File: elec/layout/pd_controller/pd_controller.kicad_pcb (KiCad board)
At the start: 2 copper layers, 26.4 x 17.6 mm, 17 parts, among them Q1 MOSFET, U1 STUSB4500QTR

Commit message: layout 95%
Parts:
- moved Q1 47.5 mm to (168.4, 57.5)
- moved R2 47.5 mm to (169.1, 66.6)
- moved R7 47.5 mm to (174.1, 61.5)
- moved U1 47.5 mm to (171.0, 63.2)
- moved C1 47.5 mm to (164.7, 54.3)
- moved C2 47.5 mm to (174.1, 60.3)
- moved D1 47.5 mm to (167.9, 60.4)
- moved R6 47.5 mm to (174.1, 62.6)
- moved USB1 47.5 mm to (163.0, 60.2)
- moved R1 47.5 mm to (171.2, 66.6)
- moved C3 47.5 mm to (171.4, 60.0)
- moved C4 47.5 mm to (170.4, 60.0)
- moved D2 47.5 mm to (167.5, 55.0)
- moved D3 47.5 mm to (170.5, 55.0)
- moved R4 47.5 mm to (172.9, 60.3)
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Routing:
- net VBUS: track 22.2 -> 0.00 mm, vias 11 -> 0
- net (no net): track 22.2 -> 0.00 mm, vias 2 -> 0
- net I2C_SCL: track 15.2 -> 0.00 mm, vias 2 -> 0
- net lv: track 12.7 -> 0.00 mm, vias 30 -> 0
- net I2C_SDA: track 11.6 -> 0.00 mm, vias 2 -> 0
- net 32: track 0.00 -> 9.23 mm
- net VSINK_VCC: track 7.14 -> 0.00 mm
- net CC2: track 5.99 -> 0.00 mm
- net CC1: track 5.72 -> 0.00 mm
- net 36: track 0.00 -> 4.51 mm
- net 31: track 0.00 -> 3.80 mm
- net 27: track 0.00 -> 2.86 mm
- net 28: track 0.00 -> 2.83 mm
- net USB_CONNECTOR-net-1: track 2.72 -> 0.00 mm
- net USB_CONNECTOR-net: track 2.72 -> 0.00 mm
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
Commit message: Build full
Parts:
- removed USB1: TYPE_C_16PIN_2MD073, lcsc:USB-C-SMD_TYPE-C-6PIN-2MD-073
- C2: value 100nF ±10% 10V X5R -> 1µF ±10% 10V X5R; footprint lcsc:C0201 -> lcsc:C0402
- C3: value 1µF ±20% 6.3V X5R -> 1µF ±10% 10V X5R; footprint lcsc:C0201 -> lcsc:C0402
- C4: value (none) -> 100nF ±10% 16V X7R; footprint lcsc:C0201 -> lcsc:C0402
- D2, D3: value (none) -> infV
- Q1: footprint lcsc:SOT-23-3_L2.9-W1.3-P1.90-LS2.4-BR -> lcsc:PDFN3333-8_L3.1-W3.2-P0.65-LS3.4-BL
- R1: value 1kΩ ±1% 50mW -> 1kΩ ±1% 62.5mW; footprint lcsc:R0201 -> lcsc:R0402
- R2: value 4.64kΩ ±1% 50mW -> 4.7kΩ ±1% 62.5mW; footprint lcsc:R0201 -> lcsc:R0402
- R3: value (none) -> 4.7kΩ ±1% 62.5mW; footprint lcsc:R0201 -> lcsc:R0402
- R4: value (none) -> 1kΩ ±1% 62.5mW; footprint lcsc:R0201 -> lcsc:R0402
- R5: value 100kΩ ±1% 50mW -> 100kΩ ±1% 62.5mW; footprint lcsc:R0201 -> lcsc:R0402
- R6: value 22.1kΩ ±1% 50mW -> 22kΩ ±1% 62.5mW; footprint lcsc:R0201 -> lcsc:R0402
- R7: value 100Ω ±1% 50mW -> 100Ω ±1% 62.5mW; footprint lcsc:R0201 -> lcsc:R0402
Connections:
- net I2C_SCL renamed signal-1
- net I2C_SDA renamed signal
- net PD_CONTROLLER.footprint.pins[18].net-net renamed pd_controller.footprint.pins[18].net-net
- C2 pad 1: net-4 -> lv
- C2 pad 2: VBUS -> VREG_1V2
- C3 pad 2: VREG_1V2 -> VREG_2V7
- C4 pad 1: lv -> net-3
- C4 pad 2: VREG_2V7 -> VBUS
- Q1 pad 1: net-3 -> VBUS
- Q1 pad 3: VSINK_VCC -> VBUS
- R1 pad 2: net-1 -> net-4
- R5 pad 1: net-3 -> net
- R6 pad 1: net-3 -> net
- R6 pad 2: net -> net-1
- R7 pad 1: net-3 -> net
- R7 pad 2: net-4 -> net-3
- U1 pad 1: CC1 -> pd_controller-signal-1
- U1 pad 16: net -> net-1
- U1 pad 5: CC2 -> pd_controller-signal
- U1 pad 9: net-1 -> net-4

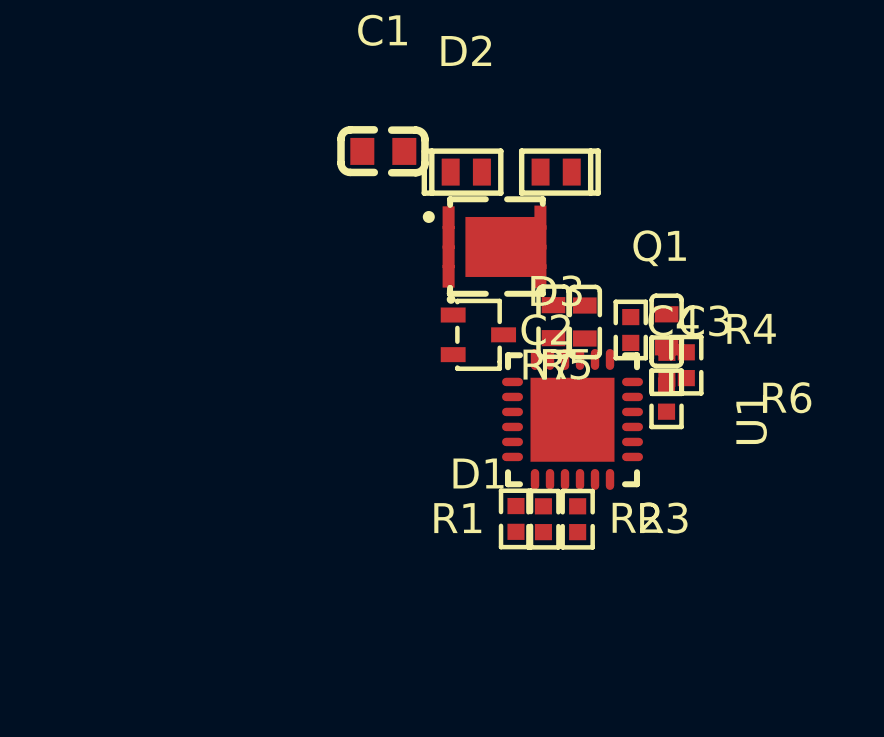
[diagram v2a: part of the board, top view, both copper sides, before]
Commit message: Don't update PCB files
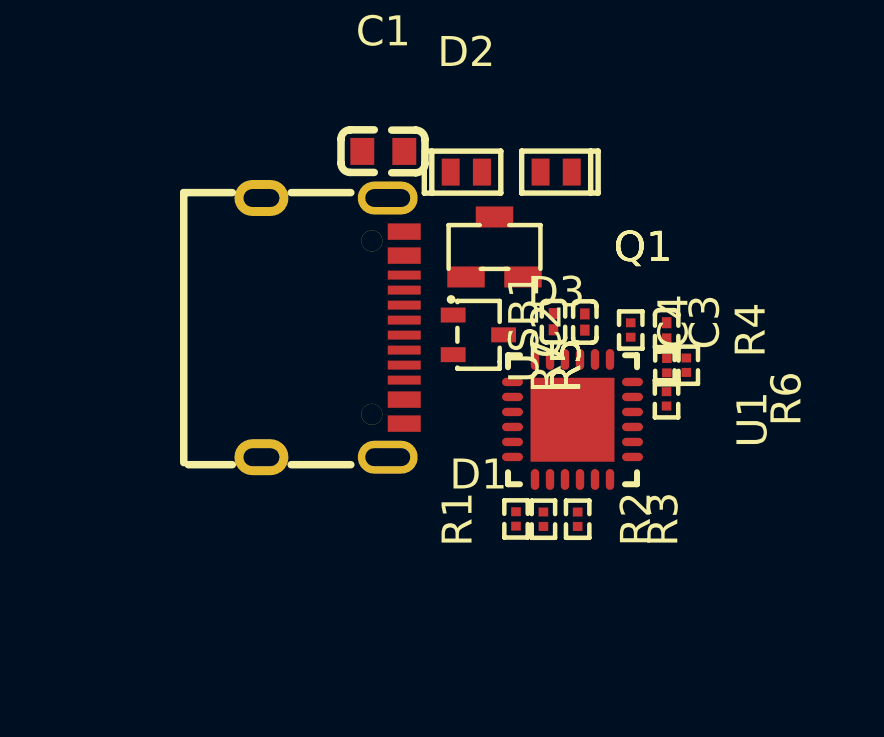
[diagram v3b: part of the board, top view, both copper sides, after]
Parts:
- added USB1: TYPE_C_16PIN_2MD073, lcsc:USB-C-SMD_TYPE-C-6PIN-2MD-073, F.Cu at (163.0, 60.2)
- C2: value 1µF ±10% 10V X5R -> 100nF ±10% 10V X5R; footprint lcsc:C0402 -> lcsc:C0201
- C3: value 1µF ±10% 10V X5R -> 1µF ±20% 6.3V X5R; footprint lcsc:C0402 -> lcsc:C0201
- C4: value 100nF ±10% 16V X7R -> (none); footprint lcsc:C0402 -> lcsc:C0201
- D2, D3: value infV -> (none)
- Q1: footprint lcsc:PDFN3333-8_L3.1-W3.2-P0.65-LS3.4-BL -> lcsc:SOT-23-3_L2.9-W1.3-P1.90-LS2.4-BR
- R1: value 1kΩ ±1% 62.5mW -> 1kΩ ±1% 50mW; footprint lcsc:R0402 -> lcsc:R0201
- R2: value 4.7kΩ ±1% 62.5mW -> 4.64kΩ ±1% 50mW; footprint lcsc:R0402 -> lcsc:R0201
- R3: value 4.7kΩ ±1% 62.5mW -> (none); footprint lcsc:R0402 -> lcsc:R0201
- R4: value 1kΩ ±1% 62.5mW -> (none); footprint lcsc:R0402 -> lcsc:R0201
- R5: value 100kΩ ±1% 62.5mW -> 100kΩ ±1% 50mW; footprint lcsc:R0402 -> lcsc:R0201
- R6: value 22kΩ ±1% 62.5mW -> 22.1kΩ ±1% 50mW; footprint lcsc:R0402 -> lcsc:R0201
- R7: value 100Ω ±1% 62.5mW -> 100Ω ±1% 50mW; footprint lcsc:R0402 -> lcsc:R0201
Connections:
- net pd_controller.footprint.pins[18].net-net renamed PD_CONTROLLER.footprint.pins[18].net-net
- net signal renamed I2C_SDA
- net signal-1 renamed I2C_SCL
- C2 pad 1: lv -> net-4
- C2 pad 2: VREG_1V2 -> VBUS
- C3 pad 2: VREG_2V7 -> VREG_1V2
- C4 pad 1: net-3 -> lv
- C4 pad 2: VBUS -> VREG_2V7
- Q1 pad 1: VBUS -> net-3
- Q1 pad 3: VBUS -> VSINK_VCC
- R1 pad 2: net-4 -> net-1
- R5 pad 1: net -> net-3
- R6 pad 1: net -> net-3
- R6 pad 2: net-1 -> net
- R7 pad 1: net -> net-3
- R7 pad 2: net-3 -> net-4
- U1 pad 1: pd_controller-signal-1 -> CC1
- U1 pad 16: net-1 -> net
- U1 pad 5: pd_controller-signal -> CC2
- U1 pad 9: net-4 -> net-1
